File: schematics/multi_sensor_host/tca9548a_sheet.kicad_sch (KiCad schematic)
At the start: 39 parts, among them J1 CONN_01X04, J2 CONN_01X04, J3 CONN_01X04, J4 CONN_01X04, J5 CONN_01X04, J6 CONN_01X04, J7 CONN_01X04, J8 CONN_01X04, U1 TCA9548A_TSSOP

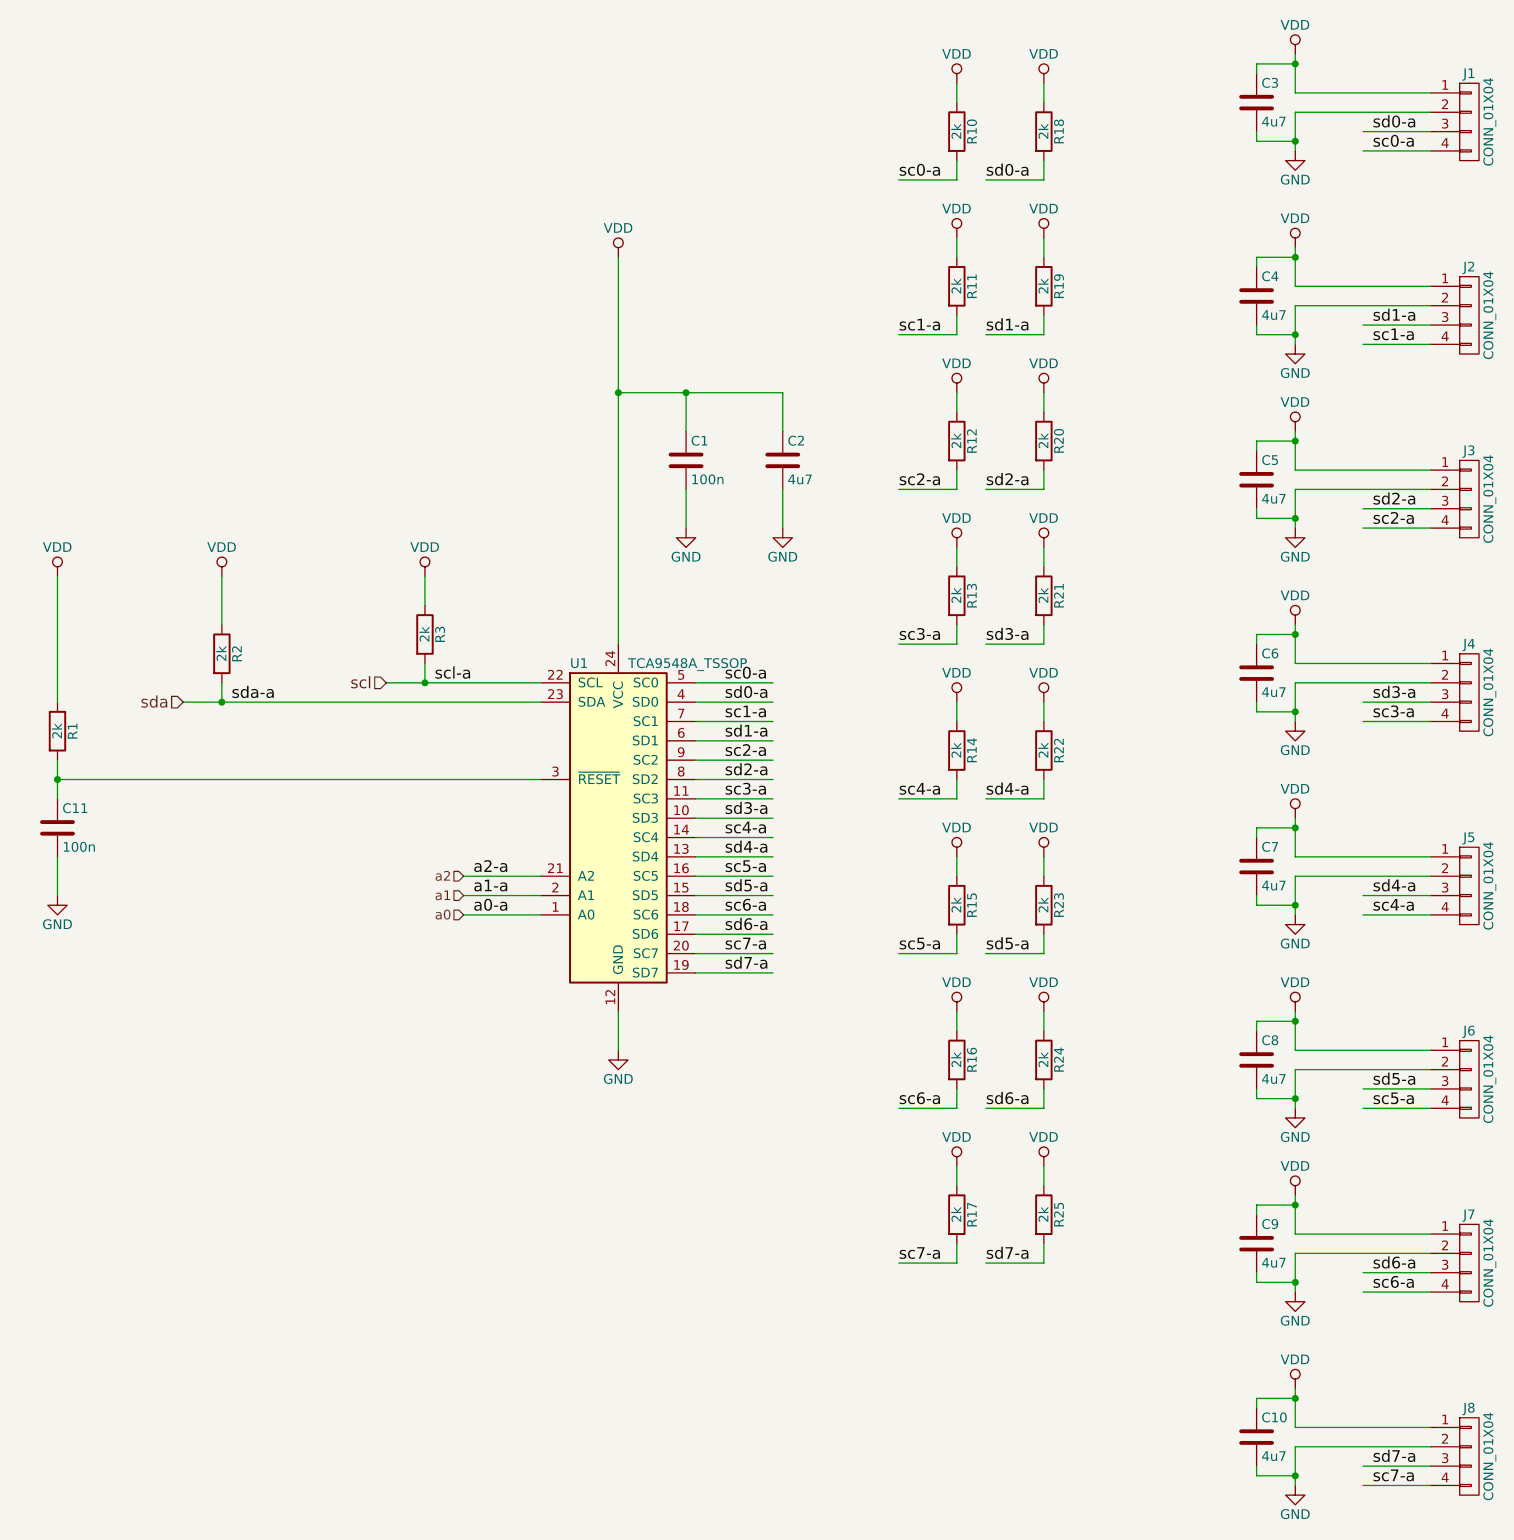
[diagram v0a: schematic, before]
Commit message: 4 shift registers are added.
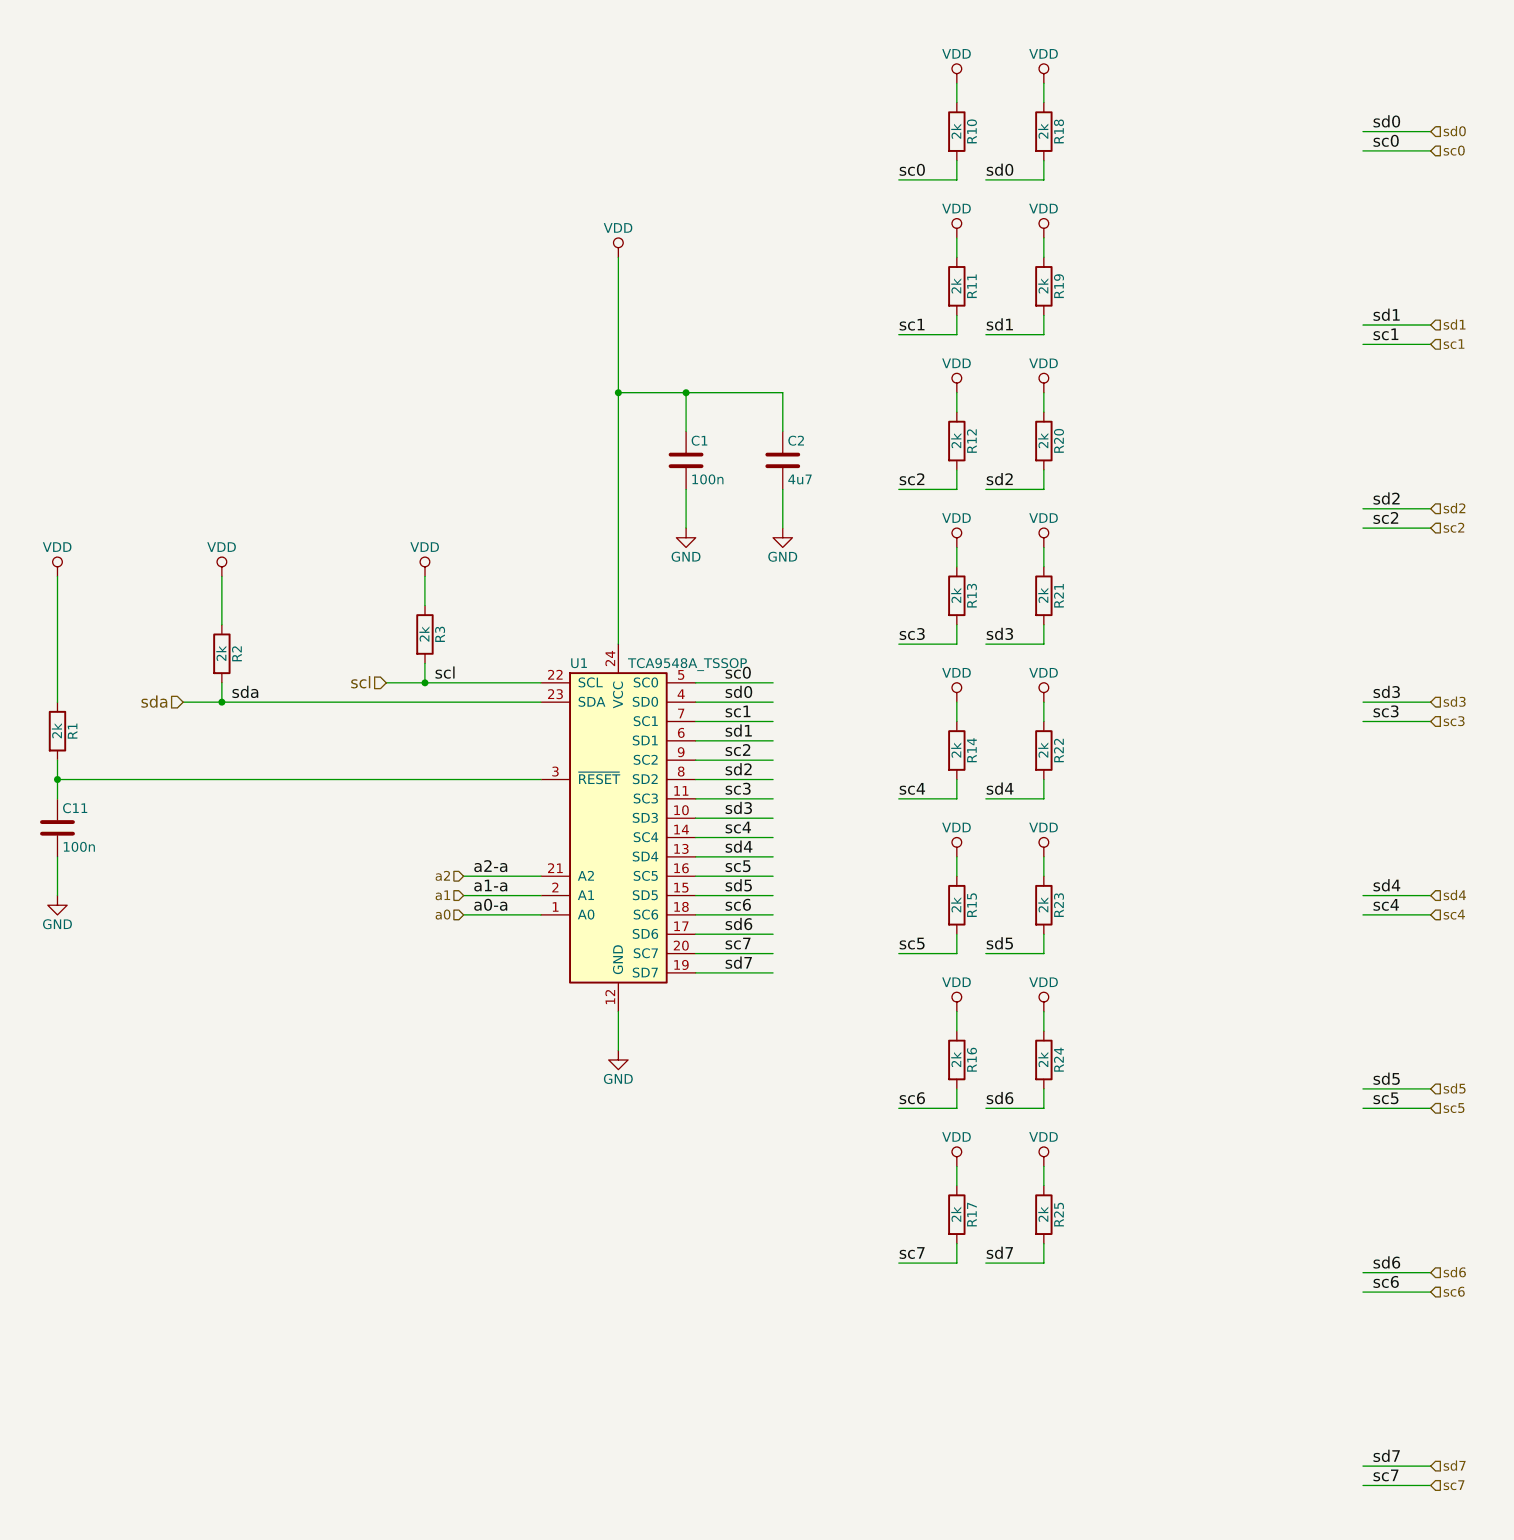
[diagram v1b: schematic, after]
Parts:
- removed C10, C3, C4, C5, C6, C7, C8, C9: 4u7, Capacitors_SMD:C_0603, symbol multi_i2c-rescue:C
- removed J1, J2, J3, J4, J5, J6, J7, J8: CONN_01X04, Pin_Headers:Pin_Header_Straight_1x04_Pitch1.27mm, symbol multi_i2c-rescue:CONN_01X04
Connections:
- net sc0-a renamed sc0
- net sc1-a renamed sc1
- net sc2-a renamed sc2
- net sc3-a renamed sc3
- net sc4-a renamed sc4
- net sc5-a renamed sc5
- net sc6-a renamed sc6
- net sc7-a renamed sc7
- net sd0-a renamed sd0
- net sd1-a renamed sd1
- net sd2-a renamed sd2
- net sd3-a renamed sd3
- net sd4-a renamed sd4
- net sd5-a renamed sd5
- net sd6-a renamed sd6
- net sd7-a renamed sd7

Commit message: Cannot re-save stm32f405rgt6. May be need to copy it again from the other project.
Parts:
- C1, C11, C2: symbol multi_i2c-rescue:C -> Device:C
- R1, R10, R11, R12, R13, R14, R15, R16, R17, R18, R19, R2, R20, R21, R22, R23, R24, R25, R3: symbol multi_i2c-rescue:R -> Device:R

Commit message: No errors, no warnings.
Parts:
- U1: symbol multi_i2c-rescue:TCA9548A_TSSOP -> tca9548a_tssop:TCA9548A_TSSOP
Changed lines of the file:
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@@
 		)
 	)
-	(label "scl"
-		(at 144.78 120.65 0)
-		(fields_autoplaced yes)
-		(effects
-			(font
-				(size 1.524 1.524)
-			)
-			(justify left bottom)
-		)
-	)
 	(label "sc5"
 		(at 205.74 156.21 0)
@@
 		)
 	)
-	(label "a0-a"
-		(at 149.86 151.13 0)
-		(fields_autoplaced yes)
-		(effects
-			(font
-				(size 1.524 1.524)
-			)
-			(justify left bottom)
-		)
-	)
-	(label "a1-a"
-		(at 149.86 148.59 0)
-		(fields_autoplaced yes)
-		(effects
-			(font
-				(size 1.524 1.524)
-			)
-			(justify left bottom)
-		)
-	)
 	(label "sc0"
 		(at 205.74 54.61 0)
@@
 		)
 	)
-	(label "a2-a"
-		(at 149.86 146.05 0)
-		(fields_autoplaced yes)
-		(effects
-			(font
-				(size 1.524 1.524)
-			)
-			(justify left bottom)
-		)
-	)
 	(label "sc1"
 		(at 267.97 76.2 0)
@@
 		)
 	)
-	(label "sda"
-		(at 118.11 123.19 0)
-		(fields_autoplaced yes)
-		(effects
-			(font
-				(size 1.524 1.524)
-			)
-			(justify left bottom)
-		)
-	)
 	(hierarchical_label "a1"
 		(shape input)
@@
 	)
 	(symbol
-		(lib_id "multi_i2c-rescue:TCA9548A_TSSOP")
+		(lib_id "tca9548a_tssop:TCA9548A_TSSOP")
 		(at 168.91 138.43 0)
 		(unit 1)
@@
 	)
 	(symbol
-		(lib_id "multi_i2c-rescue:VDD")
+		(lib_id "power:VDD")
 		(at 213.36 102.87 0)
 		(unit 1)
@@
 			)
 		)
-		(property "Description" ""
+		(property "Description" "Power symbol creates a global label with name \"VDD\""
 			(at 213.36 102.87 0)
 			(effects
@@
 	)
 	(symbol
-		(lib_id "multi_i2c-rescue:VDD")
+		(lib_id "power:VDD")
 		(at 224.79 143.51 0)
 		(unit 1)
@@
 			)
 		)
-		(property "Description" ""
+		(property "Description" "Power symbol creates a global label with name \"VDD\""
 			(at 224.79 143.51 0)
 			(effects
@@
 	)
 	(symbol
-		(lib_id "multi_i2c-rescue:VDD")
+		(lib_id "power:VDD")
 		(at 213.36 184.15 0)
 		(unit 1)
@@
 			)
 		)
-		(property "Description" ""
+		(property "Description" "Power symbol creates a global label with name \"VDD\""
 			(at 213.36 184.15 0)
 			(effects
@@
 	)
 	(symbol
-		(lib_id "multi_i2c-rescue:VDD")
+		(lib_id "power:VDD")
 		(at 95.25 106.68 0)
 		(unit 1)
@@
 			)
 		)
-		(property "Description" ""
+		(property "Description" "Power symbol creates a global label with name \"VDD\""
 			(at 95.25 106.68 0)
 			(effects
@@
 	)
 	(symbol
-		(lib_id "multi_i2c-rescue:VDD")
+		(lib_id "power:VDD")
 		(at 224.79 41.91 0)
 		(unit 1)
@@
 			)
 		)
-		(property "Description" ""
+		(property "Description" "Power symbol creates a global label with name \"VDD\""
 			(at 224.79 41.91 0)
 			(effects
@@
 	)
 	(symbol
-		(lib_id "multi_i2c-rescue:VDD")
+		(lib_id "power:VDD")
 		(at 224.79 102.87 0)
 		(unit 1)
@@
 			)
 		)
-		(property "Description" ""
+		(property "Description" "Power symbol creates a global label with name \"VDD\""
 			(at 224.79 102.87 0)
 			(effects
@@
 	)
 	(symbol
-		(lib_id "multi_i2c-rescue:VDD")
+		(lib_id "power:VDD")
 		(at 224.79 163.83 0)
 		(unit 1)
@@
 			)
 		)
-		(property "Description" ""
+		(property "Description" "Power symbol creates a global label with name \"VDD\""
 			(at 224.79 163.83 0)
 			(effects
@@
 	)
 	(symbol
-		(lib_id "multi_i2c-rescue:VDD")
+		(lib_id "power:VDD")
 		(at 213.36 82.55 0)
 		(unit 1)
@@
 			)
 		)
-		(property "Description" ""
+		(property "Description" "Power symbol creates a global label with name \"VDD\""
 			(at 213.36 82.55 0)
 			(effects
@@
 	)
 	(symbol
-		(lib_id "multi_i2c-rescue:VDD")
+		(lib_id "power:VDD")
 		(at 213.36 41.91 0)
 		(unit 1)
@@
 			)
 		)
-		(property "Description" ""
+		(property "Description" "Power symbol creates a global label with name \"VDD\""
 			(at 213.36 41.91 0)
 			(effects
@@
 	)
 	(symbol
-		(lib_id "multi_i2c-rescue:VDD")
+		(lib_id "power:VDD")
 		(at 224.79 82.55 0)
 		(unit 1)
@@
 			)
 		)
-		(property "Description" ""
+		(property "Description" "Power symbol creates a global label with name \"VDD\""
 			(at 224.79 82.55 0)
 			(effects
@@
 	)
 	(symbol
-		(lib_id "multi_i2c-rescue:VDD")
+		(lib_id "power:VDD")
 		(at 224.79 123.19 0)
 		(unit 1)
@@
 			)
 		)
-		(property "Description" ""
+		(property "Description" "Power symbol creates a global label with name \"VDD\""
 			(at 224.79 123.19 0)
 			(effects
@@
 	)
 	(symbol
-		(lib_id "multi_i2c-rescue:VDD")
+		(lib_id "power:VDD")
 		(at 213.36 163.83 0)
 		(unit 1)
@@
 			)
 		)
-		(property "Description" ""
+		(property "Description" "Power symbol creates a global label with name \"VDD\""
 			(at 213.36 163.83 0)
 			(effects
@@
 	)
 	(symbol
-		(lib_id "multi_i2c-rescue:VDD")
+		(lib_id "power:VDD")
 		(at 213.36 123.19 0)
 		(unit 1)
@@
 			)
 		)
-		(property "Description" ""
+		(property "Description" "Power symbol creates a global label with name \"VDD\""
 			(at 213.36 123.19 0)
 			(effects
@@
 	)
 	(symbol
-		(lib_id "multi_i2c-rescue:VDD")
+		(lib_id "power:VDD")
 		(at 213.36 143.51 0)
 		(unit 1)
@@
 			)
 		)
-		(property "Description" ""
+		(property "Description" "Power symbol creates a global label with name \"VDD\""
 			(at 213.36 143.51 0)
 			(effects
@@
 	)
 	(symbol
-		(lib_id "multi_i2c-rescue:VDD")
+		(lib_id "power:VDD")
 		(at 143.51 106.68 0)
 		(unit 1)
@@
 			)
 		)
-		(property "Description" ""
+		(property "Description" "Power symbol creates a global label with name \"VDD\""
 			(at 143.51 106.68 0)
 			(effects
@@
 	)
 	(symbol
-		(lib_id "multi_i2c-rescue:VDD")
+		(lib_id "power:VDD")
 		(at 224.79 184.15 0)
 		(unit 1)
@@
 			)
 		)
-		(property "Description" ""
+		(property "Description" "Power symbol creates a global label with name \"VDD\""
 			(at 224.79 184.15 0)
 			(effects
@@
 	)
 	(symbol
-		(lib_id "multi_i2c-rescue:VDD")
+		(lib_id "power:VDD")
 		(at 213.36 62.23 0)
 		(unit 1)
@@
 			)
 		)
-		(property "Description" ""
+		(property "Description" "Power symbol creates a global label with name \"VDD\""
 			(at 213.36 62.23 0)
 			(effects
@@
 	)
 	(symbol
-		(lib_id "multi_i2c-rescue:VDD")
+		(lib_id "power:VDD")
 		(at 224.79 62.23 0)
 		(unit 1)
@@
 			)
 		)
-		(property "Description" ""
+		(property "Description" "Power symbol creates a global label with name \"VDD\""
 			(at 224.79 62.23 0)
 			(effects
@@
 	)
 	(symbol
-		(lib_id "multi_i2c-rescue:VDD")
+		(lib_id "power:VDD")
 		(at 116.84 106.68 0)
 		(unit 1)
@@
 			)
 		)
-		(property "Description" ""
+		(property "Description" "Power symbol creates a global label with name \"VDD\""
 			(at 116.84 106.68 0)
 			(effects
@@
 	)
 	(symbol
-		(lib_id "multi_i2c-rescue:VDD")
+		(lib_id "power:VDD")
 		(at 168.91 64.77 0)
 		(unit 1)
@@
 			)
 		)
-		(property "Description" ""
+		(property "Description" "Power symbol creates a global label with name \"VDD\""
 			(at 168.91 64.77 0)
 			(effects

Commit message: Assigned footprints. Also, just in case found a chip I2C to diff. pair.
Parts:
- C1, C11, C2: footprint Capacitors_SMD:C_0603 -> Capacitor_SMD:C_0603_1608Metric
- R1, R10, R11, R12, R13, R14, R15, R16, R17, R18, R19, R2, R20, R21, R22, R23, R24, R25, R3: footprint Resistors_SMD:R_0603 -> Capacitor_SMD:C_0603_1608Metric
- U1: footprint Housings_SSOP:TSSOP-24_4.4x7.8mm_Pitch0.65mm -> Package_SO:TSSOP-24_4.4x7.8mm_P0.65mm
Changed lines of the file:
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@@
 			)
 		)
-		(property "Footprint" "Resistors_SMD:R_0603"
+		(property "Footprint" "Capacitor_SMD:C_0603_1608Metric"
 			(at 211.582 68.58 90)
 			(effects
@@
 			)
 		)
-		(property "Footprint" "Resistors_SMD:R_0603"
+		(property "Footprint" "Capacitor_SMD:C_0603_1608Metric"
 			(at 211.582 48.26 90)
 			(effects
@@
 			)
 		)
-		(property "Footprint" "Housings_SSOP:TSSOP-24_4.4x7.8mm_Pitch0.65mm"
+		(property "Footprint" "Package_SO:TSSOP-24_4.4x7.8mm_P0.65mm"
 			(at 194.31 161.29 0)
 			(effects
@@
 			)
 		)
-		(property "Footprint" "Resistors_SMD:R_0603"
+		(property "Footprint" "Capacitor_SMD:C_0603_1608Metric"
 			(at 211.582 129.54 90)
 			(effects
@@
 			)
 		)
-		(property "Footprint" "Capacitors_SMD:C_0603"
+		(property "Footprint" "Capacitor_SMD:C_0603_1608Metric"
 			(at 96.2152 143.51 0)
 			(effects
@@
 			)
 		)
-		(property "Footprint" "Resistors_SMD:R_0603"
+		(property "Footprint" "Capacitor_SMD:C_0603_1608Metric"
 			(at 223.012 48.26 90)
 			(effects
@@
 			)
 		)
-		(property "Footprint" "Resistors_SMD:R_0603"
+		(property "Footprint" "Capacitor_SMD:C_0603_1608Metric"
 			(at 93.472 127 90)
 			(effects
@@
 			)
 		)
-		(property "Footprint" "Capacitors_SMD:C_0603"
+		(property "Footprint" "Capacitor_SMD:C_0603_1608Metric"
 			(at 178.7652 95.25 0)
 			(effects
@@
 			)
 		)
-		(property "Footprint" "Resistors_SMD:R_0603"
+		(property "Footprint" "Capacitor_SMD:C_0603_1608Metric"
 			(at 223.012 109.22 90)
 			(effects
@@
 			)
 		)
-		(property "Footprint" "Resistors_SMD:R_0603"
+		(property "Footprint" "Capacitor_SMD:C_0603_1608Metric"
 			(at 223.012 88.9 90)
 			(effects
@@
 			)
 		)
-		(property "Footprint" "Resistors_SMD:R_0603"
+		(property "Footprint" "Capacitor_SMD:C_0603_1608Metric"
 			(at 141.732 114.3 90)
 			(effects
@@
 			)
 		)
-		(property "Footprint" "Resistors_SMD:R_0603"
+		(property "Footprint" "Capacitor_SMD:C_0603_1608Metric"
 			(at 115.062 116.84 90)
 			(effects
@@
 			)
 		)
-		(property "Footprint" "Resistors_SMD:R_0603"
+		(property "Footprint" "Capacitor_SMD:C_0603_1608Metric"
 			(at 211.582 109.22 90)
 			(effects
@@
 			)
 		)
-		(property "Footprint" "Resistors_SMD:R_0603"
+		(property "Footprint" "Capacitor_SMD:C_0603_1608Metric"
 			(at 211.582 149.86 90)
 			(effects
@@
 			)
 		)
-		(property "Footprint" "Resistors_SMD:R_0603"
+		(property "Footprint" "Capacitor_SMD:C_0603_1608Metric"
 			(at 211.582 190.5 90)
 			(effects
@@
 			)
 		)
-		(property "Footprint" "Resistors_SMD:R_0603"
+		(property "Footprint" "Capacitor_SMD:C_0603_1608Metric"
 			(at 223.012 129.54 90)
 			(effects
@@
 			)
 		)
-		(property "Footprint" "Resistors_SMD:R_0603"
+		(property "Footprint" "Capacitor_SMD:C_0603_1608Metric"
 			(at 223.012 68.58 90)
 			(effects
@@
 			)
 		)
-		(property "Footprint" "Resistors_SMD:R_0603"
+		(property "Footprint" "Capacitor_SMD:C_0603_1608Metric"
 			(at 211.582 170.18 90)
 			(effects
@@
 			)
 		)
-		(property "Footprint" "Resistors_SMD:R_0603"
+		(property "Footprint" "Capacitor_SMD:C_0603_1608Metric"
 			(at 211.582 88.9 90)
 			(effects
@@
 			)
 		)
-		(property "Footprint" "Capacitors_SMD:C_0603"
+		(property "Footprint" "Capacitor_SMD:C_0603_1608Metric"
 			(at 191.4652 95.25 0)
 			(effects
@@
 			)
 		)
-		(property "Footprint" "Resistors_SMD:R_0603"
+		(property "Footprint" "Capacitor_SMD:C_0603_1608Metric"
 			(at 223.012 149.86 90)
 			(effects
@@
 			)
 		)
-		(property "Footprint" "Resistors_SMD:R_0603"
+		(property "Footprint" "Capacitor_SMD:C_0603_1608Metric"
 			(at 223.012 170.18 90)
 			(effects
@@
 			)
 		)
-		(property "Footprint" "Resistors_SMD:R_0603"
+		(property "Footprint" "Capacitor_SMD:C_0603_1608Metric"
 			(at 223.012 190.5 90)
 			(effects

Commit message: Assigning URLs.
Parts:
- U1: URL (none) -> https://www.digikey.com/product-detail/en/texas-instruments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; url https://www.digikey.com/product-detail/en/texas-instruments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 -> (none)
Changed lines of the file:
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@@
 			)
 		)
-		(property "url" "https://www.digikey.com/product-detail/en/texas-instruments/TCA9548APWR/296-34905-1-ND/3615448"
+		(property "URL" "https://www.digikey.com/product-detail/en/texas-instruments/TCA9548APWR/296-34905-1-ND/3615448"
 			(at 168.91 138.43 0)
 			(effects
